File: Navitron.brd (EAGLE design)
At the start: 70 x 70 mm, 92 parts, among them J2 DX07S016JA1R1500, Q1 ROHM_RUM002N02T2LROHM_RUM002N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, Q2 2.5A/30V, Q3 ROHM_RUM002N02T2LROHM_RUM002N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, Q4 ROHM_RUM002N02T2LROHM_RUM002N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, Q5 ROHM_RUM002N02T2LROHM_RUM002N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, T1 BC847, T2 BC847, U3 MCP73831, U5 CH340C

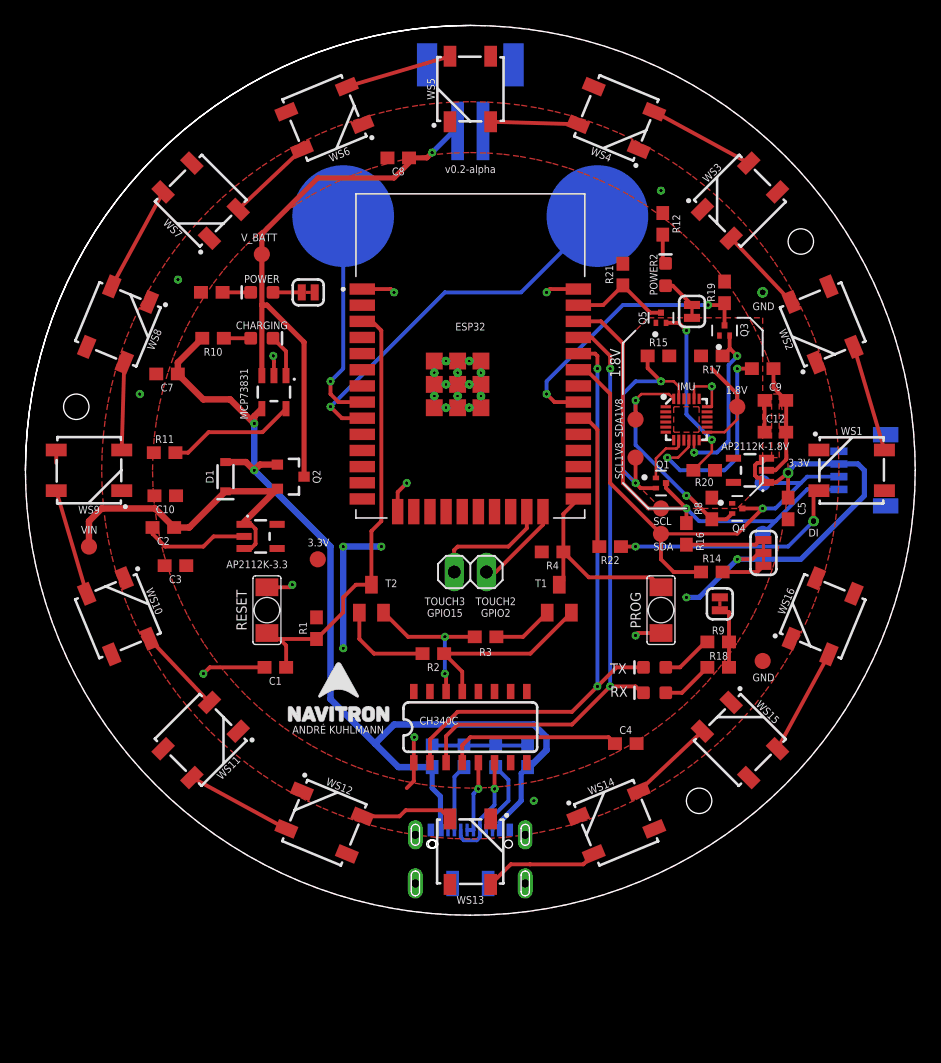
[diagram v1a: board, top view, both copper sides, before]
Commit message: Add Additional 1.8V SDA and SCL Pad
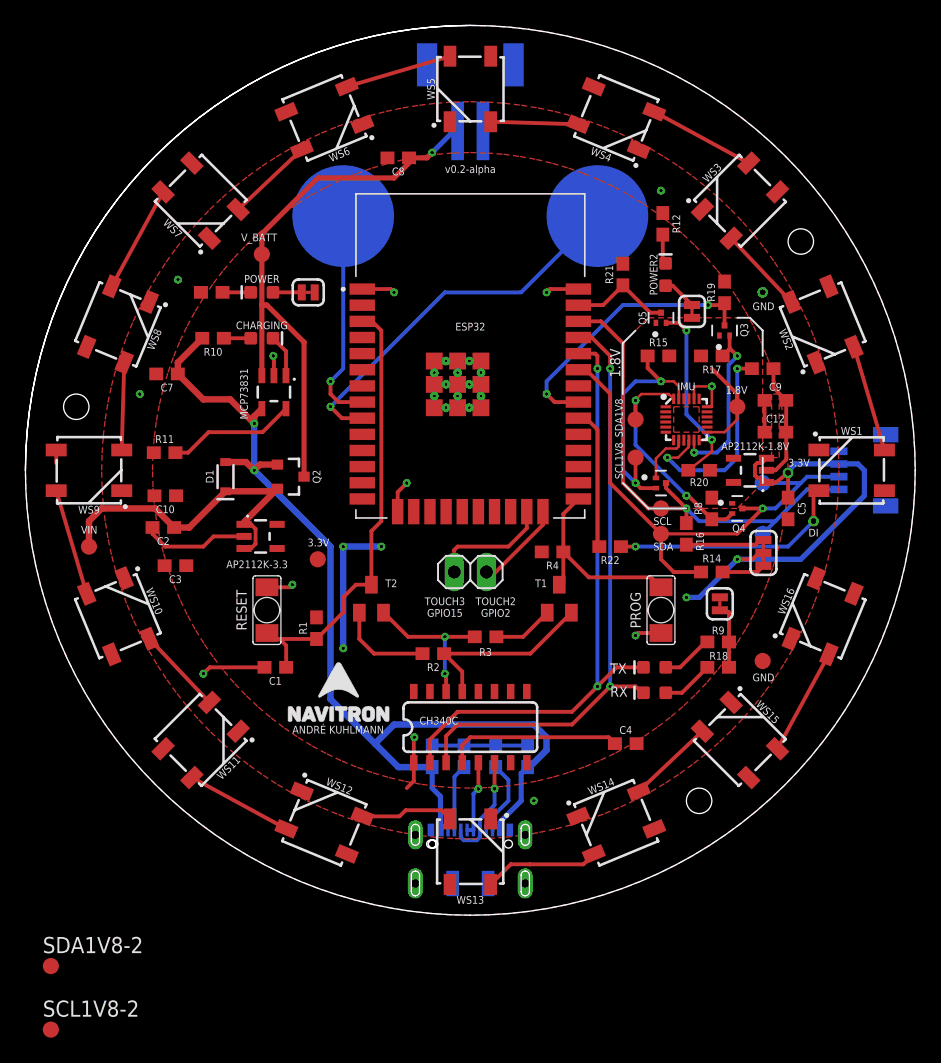
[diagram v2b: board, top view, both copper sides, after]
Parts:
- added SCL1V8-2, SDA1V8-2: PTR1B1,27, testpad:B1,27
- moved R20 0.40 mm to (53.0, 35.0)
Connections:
- net SCL1V8: now also SCL1V8-2.TP
- net SDA1V8: now also SDA1V8-2.TP
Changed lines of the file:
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@@
 <grid distance="1" unitdist="mm" unit="mm" style="lines" multiple="1" display="yes" altdistance="5" altunitdist="mil" altunit="mil"/>
 <layers>
-<layer number="1" name="Top" color="4" fill="1" visible="yes" active="yes"/>
+<layer number="1" name="Top" color="4" fill="1" visible="no" active="yes"/>
 <layer number="2" name="Route2" color="16" fill="1" visible="no" active="no"/>
 <layer number="3" name="Route3" color="17" fill="1" visible="no" active="no"/>
@@
 <layer number="19" name="Unrouted" color="6" fill="1" visible="yes" active="yes"/>
 <layer number="20" name="Dimension" color="24" fill="1" visible="yes" active="yes"/>
-<layer number="21" name="tPlace" color="7" fill="1" visible="yes" active="yes"/>
-<layer number="22" name="bPlace" color="7" fill="1" visible="no" active="yes"/>
-<layer number="23" name="tOrigins" color="15" fill="1" visible="yes" active="yes"/>
-<layer number="24" name="bOrigins" color="15" fill="1" visible="no" active="yes"/>
-<layer number="25" name="tNames" color="7" fill="1" visible="yes" active="yes"/>
-<layer number="26" name="bNames" color="7" fill="1" visible="no" active="yes"/>
+<layer number="21" name="tPlace" color="7" fill="1" visible="no" active="yes"/>
+<layer number="22" name="bPlace" color="7" fill="1" visible="yes" active="yes"/>
+<layer number="23" name="tOrigins" color="15" fill="1" visible="no" active="yes"/>
+<layer number="24" name="bOrigins" color="15" fill="1" visible="yes" active="yes"/>
+<layer number="25" name="tNames" color="7" fill="1" visible="no" active="yes"/>
+<layer number="26" name="bNames" color="7" fill="1" visible="yes" active="yes"/>
 <layer number="27" name="tValues" color="7" fill="1" visible="no" active="yes"/>
 <layer number="28" name="bValues" color="7" fill="1" visible="no" active="yes"/>
@@
 <layer number="37" name="tTest" color="7" fill="1" visible="no" active="yes"/>
 <layer number="38" name="bTest" color="7" fill="1" visible="no" active="yes"/>
-<layer number="39" name="tKeepout" color="4" fill="11" visible="yes" active="yes"/>
-<layer number="40" name="bKeepout" color="1" fill="11" visible="no" active="yes"/>
-<layer number="41" name="tRestrict" color="4" fill="10" visible="yes" active="yes"/>
-<layer number="42" name="bRestrict" color="1" fill="10" visible="no" active="yes"/>
+<layer number="39" name="tKeepout" color="4" fill="11" visible="no" active="yes"/>
+<layer number="40" name="bKeepout" color="1" fill="11" visible="yes" active="yes"/>
+<layer number="41" name="tRestrict" color="4" fill="10" visible="no" active="yes"/>
+<layer number="42" name="bRestrict" color="1" fill="10" visible="yes" active="yes"/>
 <layer number="43" name="vRestrict" color="2" fill="10" visible="no" active="yes"/>
 <layer number="44" name="Drills" color="7" fill="1" visible="no" active="yes"/>
@@
 <layer number="49" name="Reference" color="7" fill="1" visible="no" active="yes"/>
 <layer number="50" name="dxf" color="7" fill="1" visible="no" active="no"/>
-<layer number="51" name="tDocu" color="7" fill="1" visible="yes" active="yes"/>
-<layer number="52" name="bDocu" color="7" fill="1" visible="no" active="yes"/>
+<layer number="51" name="tDocu" color="7" fill="1" visible="no" active="yes"/>
+<layer number="52" name="bDocu" color="7" fill="1" visible="yes" active="yes"/>
 <layer number="53" name="tGND_GNDA" color="7" fill="9" visible="no" active="no"/>
 <layer number="54" name="bGND_GNDA" color="1" fill="9" visible="no" active="no"/>
@@
 <wire x1="47" y1="34" x2="49" y2="32" width="0.15" layer="25"/>
 <wire x1="49" y1="32" x2="52" y2="32" width="0.15" layer="25"/>
-<wire x1="57" y1="33" x2="58" y2="34" width="0.15" layer="25"/>
 <wire x1="58" y1="34" x2="58" y2="36" width="0.15" layer="25"/>
 <wire x1="56" y1="47" x2="57" y2="47" width="0.15" layer="25"/>
@@
 <attribute name="MOUSER_PART_NUMBER" value="755-RUM002N02T2L" x="50" y="34" size="1.778" layer="27" display="off"/>
 <attribute name="MPN" value="RUM002N02T2L" x="50" y="34" size="1.778" layer="27" display="off"/>
-<attribute name="NAME" x="49.6" y="35.15" size="0.6096" layer="25" ratio="20"/>
 <attribute name="PACKAGE" value="SOT-23" x="50" y="34" size="1.778" layer="27" display="off"/>
 <attribute name="PREFIX" value="Q" x="50" y="34" size="1.778" layer="27" display="off"/>
@@
 <attribute name="VALUE" x="51.238" y="30" size="0.6096" layer="27" font="vector" ratio="20" rot="R270" align="top-center"/>
 </element>
-<element name="R20" library="SparkFun-Resistors" package="0603" value="2.2k" x="53.4" y="35" smashed="yes">
-<attribute name="NAME" x="53.4" y="33.762" size="0.6096" layer="25" font="vector" ratio="20" align="bottom-center"/>
-<attribute name="PROD_ID" value="RES-12083" x="53.4" y="35" size="1.778" layer="27" display="off"/>
-<attribute name="VALUE" x="53.4" y="34.238" size="0.6096" layer="27" font="vector" ratio="20" align="top-center"/>
+<element name="R20" library="SparkFun-Resistors" package="0603" value="2.2k" x="53" y="35" smashed="yes">
+<attribute name="NAME" x="53" y="33.762" size="0.6096" layer="25" font="vector" ratio="20" align="bottom-center"/>
+<attribute name="PROD_ID" value="RES-12083" x="53" y="35" size="1.778" layer="27" display="off"/>
+<attribute name="VALUE" x="53" y="34.238" size="0.6096" layer="27" font="vector" ratio="20" align="top-center"/>
 </element>
 <element name="R21" library="SparkFun-Resistors" package="0603" value="2.2k" x="47" y="50.4" smashed="yes" rot="R90">
@@
 <attribute name="POPULARITY" value="98" x="35" y="27" size="0.6096" layer="27" ratio="20" rot="R180" display="off"/>
 <attribute name="VALUE" x="37.54" y="30.175" size="1.27" layer="27" rot="R180"/>
+</element>
+<element name="SDA1V8-2" library="testpad" library_urn="urn:adsk.eagle:library:385" package="B1,27" package3d_urn="urn:adsk.eagle:package:27944/2" value="PTR1B1,27" x="2" y="-4" smashed="yes">
+<attribute name="NAME" x="1.365" y="-2.984" size="1.27" layer="25" ratio="10"/>
+<attribute name="POPULARITY" value="2" x="2" y="-4" size="0.6096" layer="27" ratio="20" display="off"/>
+<attribute name="TP_SIGNAL_NAME" value="" x="1.365" y="-5.905" size="1" layer="37"/>
+<attribute name="VALUE" x="1.365" y="-4.762" size="0.0254" layer="27"/>
+</element>
+<element name="SCL1V8-2" library="testpad" library_urn="urn:adsk.eagle:library:385" package="B1,27" package3d_urn="urn:adsk.eagle:package:27944/2" value="PTR1B1,27" x="2" y="-9" smashed="yes">
+<attribute name="NAME" x="1.365" y="-7.984" size="1.27" layer="25" ratio="10"/>
+<attribute name="POPULARITY" value="2" x="2" y="-9" size="0.6096" layer="27" ratio="20" display="off"/>
+<attribute name="TP_SIGNAL_NAME" value="" x="1.365" y="-10.905" size="1" layer="37"/>
+<attribute name="VALUE" x="1.365" y="-9.762" size="0.0254" layer="27"/>
 </element>
 </elements>
@@
 <contactref element="JP3" pad="1"/>
 <contactref element="C9" pad="1"/>
-<polygon width="0.15" layer="1">
-<vertex x="49" y="47"/>
-<vertex x="58" y="47"/>
-<vertex x="58" y="34"/>
-<vertex x="56" y="32"/>
-<vertex x="50" y="32"/>
-<vertex x="47" y="35"/>
-<vertex x="47" y="45"/>
-</polygon>
 <contactref element="C12" pad="1"/>
 <contactref element="Q4" pad="1"/>
@@
 <contactref element="IMU" pad="13"/>
 <contactref element="IMU" pad="8"/>
+<wire x1="53.6256" y1="38" x2="55" y2="38" width="0.2032" layer="1"/>
+<wire x1="55" y1="38" x2="56" y2="39" width="0.2032" layer="1"/>
+<wire x1="56" y1="39" x2="56" y2="40" width="0.2032" layer="1"/>
+<polygon width="0.15" layer="1">
+<vertex x="47" y="45"/>
+<vertex x="49" y="47"/>
+<vertex x="57" y="47"/>
+<vertex x="58" y="46"/>
+<vertex x="58" y="34"/>
+<vertex x="56" y="32"/>
+<vertex x="49" y="32"/>
+<vertex x="47" y="34"/>
+</polygon>
 <wire x1="51.4" y1="37.3744" x2="51.379" y2="37.3534" width="0.2032" layer="1"/>
 <wire x1="51.379" y1="37.3534" x2="51.379" y2="36.8627875" width="0.2032" layer="1"/>
@@
 <wire x1="49.6" y1="35.92335625" x2="49.6" y2="34.4" width="0.2032" layer="1"/>
 <wire x1="51.2302125" y1="36.714" x2="50.39064375" y2="36.714" width="0.2032" layer="1"/>
-<wire x1="53.6256" y1="38" x2="55" y2="38" width="0.2032" layer="1"/>
-<wire x1="55" y1="38" x2="56" y2="39" width="0.2032" layer="1"/>
-<wire x1="56" y1="39" x2="56" y2="40" width="0.2032" layer="1"/>
 </signal>
 <signal name="N$8">
@@
 <wire x1="48.4475" y1="41" x2="48" y2="40.5525" width="0.2032" layer="1"/>
 <wire x1="50.625603125" y1="41" x2="48.4475" y2="41" width="0.2032" layer="1"/>
+<contactref element="SDA1V8-2" pad="TP"/>
+<wire x1="2" y1="-4" x2="52" y2="33" width="0" layer="19" extent="1-1"/>
 </signal>
 <signal name="SCL1V8">
@@
 <wire x1="51.4" y1="41.6" x2="51" y2="42" width="0.2032" layer="1"/>
 <wire x1="51" y1="42" x2="50" y2="42" width="0.2032" layer="1"/>
+<contactref element="SCL1V8-2" pad="TP"/>
+<wire x1="2" y1="-9" x2="48" y2="34" width="0" layer="19" extent="1-1"/>
 </signal>
 <signal name="DI">
@@
 <wire x1="53.938196875" y1="37.3744" x2="53" y2="37.3744" width="0.2032" layer="1"/>
 <wire x1="54" y1="37.4" x2="54" y2="36.45" width="0.2032" layer="1"/>
-<wire x1="54" y1="36.45" x2="52.55" y2="35" width="0.2032" layer="1"/>
+<wire x1="54" y1="36.45" x2="52.15" y2="35" width="0.2032" layer="1"/>
 </signal>
 <signal name="FSYNC_VIN">

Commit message: Change Bottom Logo Position
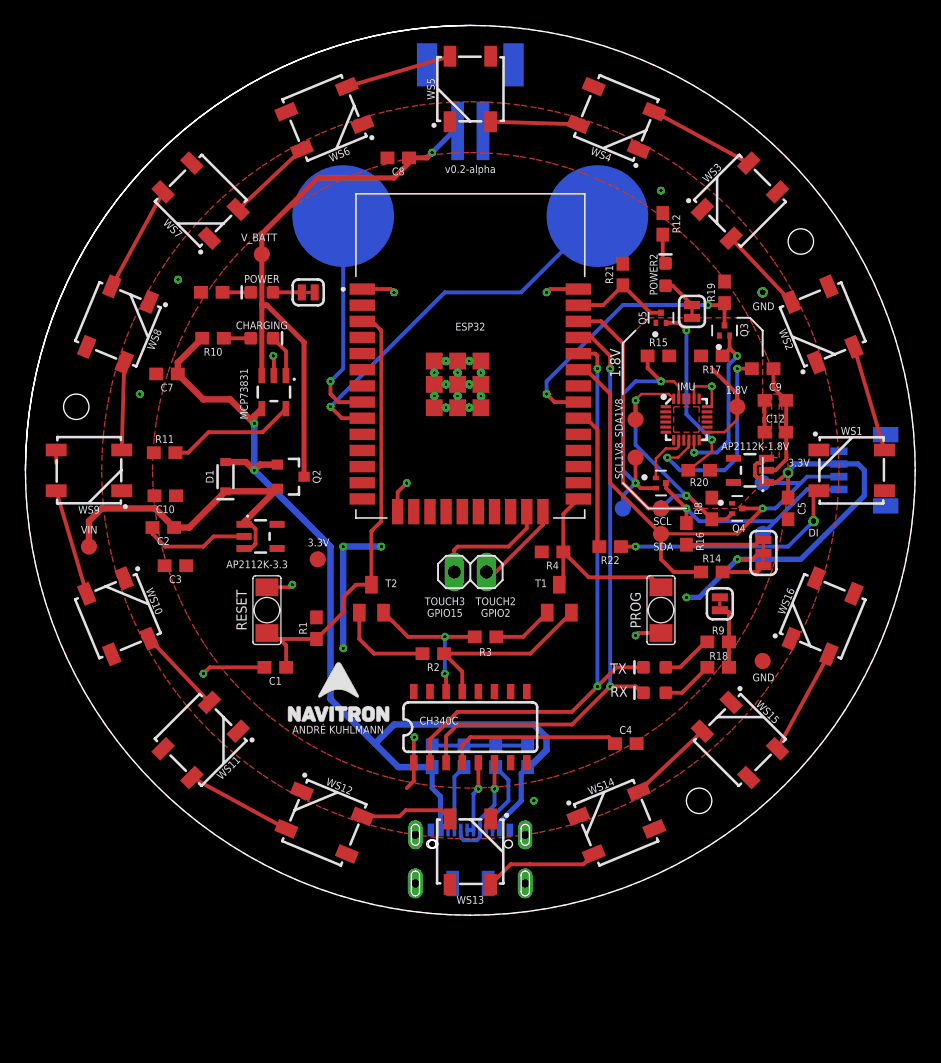
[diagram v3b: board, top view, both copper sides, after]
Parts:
- moved SCL1V8-2 60.9 mm to (47.0, 32.0), flipped to the bottom
- moved SDA1V8-2 60.0 mm to (50.0, 32.0), flipped to the bottom
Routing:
- net SDA1V8: track 18.6 -> 21.0 mm
- net SCL1V8: track 19.6 -> 22.0 mm
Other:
- board text added: "SCL1.8"
- board text added: "SDA1.8"

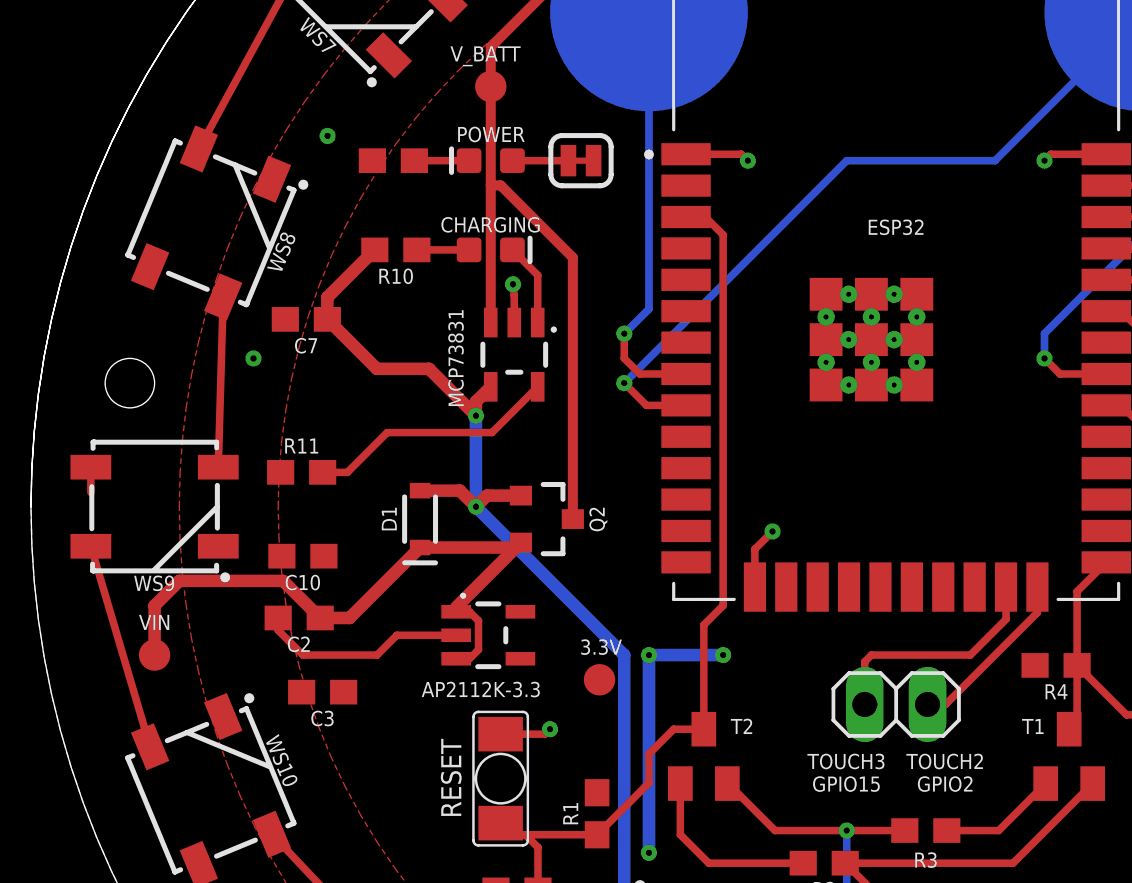
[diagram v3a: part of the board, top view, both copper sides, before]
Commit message: Cleanup 3.3V Power Circuit
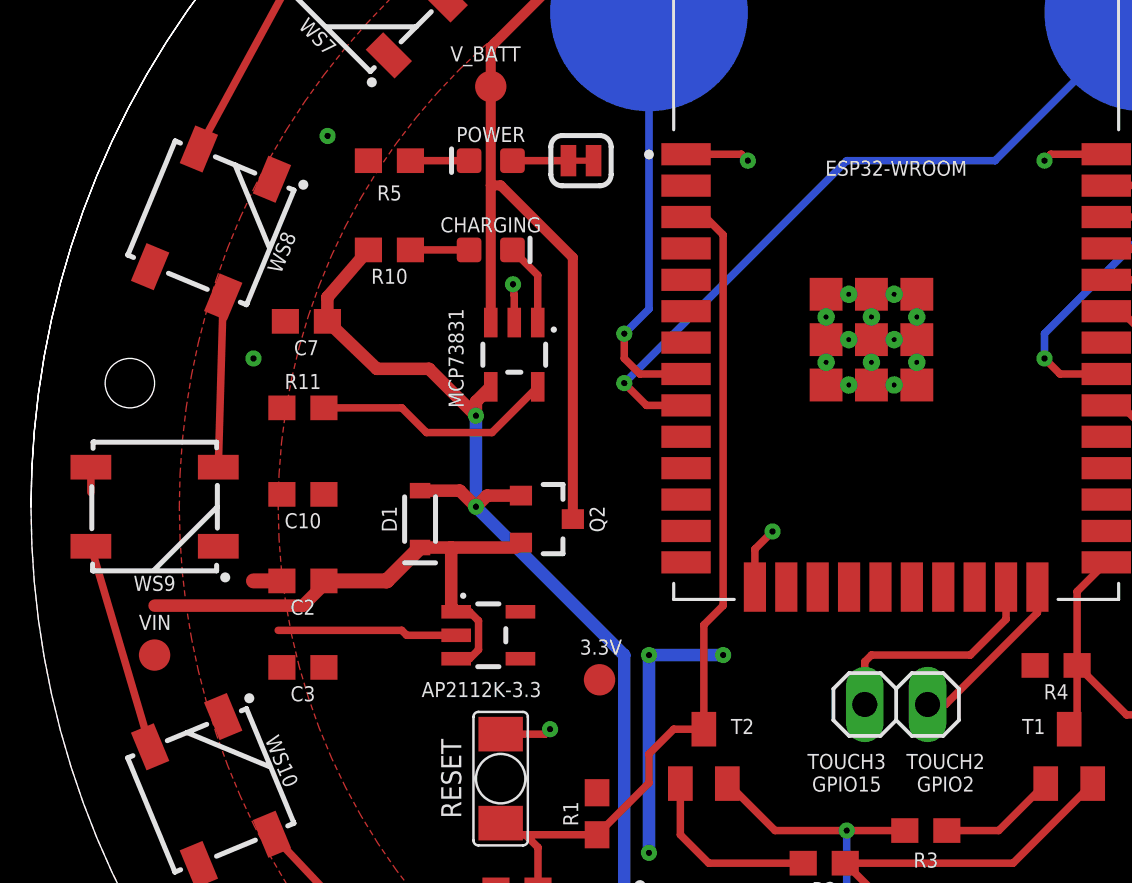
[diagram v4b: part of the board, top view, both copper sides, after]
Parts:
- moved R11 2.61 mm to (11.0, 39.0)
- moved C10 2.50 mm to (11.0, 35.5)
- moved C2 1.51 mm to (11.0, 32.0)
- moved C3 1.28 mm to (11.0, 28.5)
- moved R10 0.26 mm to (14.5, 45.4)
- moved R5 0.16 mm to (14.5, 49.0)
- moved C7 0.08 mm to (11.1, 42.5)
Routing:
- net VIN: track 27.3 -> 23.0 mm
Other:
- board text added: "ESP32-WROOM"
- board text added: "R5"

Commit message: Small changes
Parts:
- CHARGING: value RED -> GREEN
- RX1, TX1: value YELLOW -> BLUE
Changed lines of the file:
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@@
 <drawing>
 <settings>
-<setting alwaysvectorfont="yes"/>
+<setting alwaysvectorfont="no"/>
 <setting verticaltext="up"/>
 </settings>
@@
 <attribute name="VALUE" x="59" y="39.738" size="0.6096" layer="27" font="vector" ratio="20" align="top-center"/>
 </element>
-<element name="CHARGING" library="SparkFun-LED" package="LED-0603" value="RED" x="18.6" y="45.39" smashed="yes">
+<element name="CHARGING" library="SparkFun-LED" package="LED-0603" value="GREEN" x="18.6" y="45.39" smashed="yes">
 <attribute name="NAME" x="18.6" y="46.1" size="0.6096" layer="25" font="vector" ratio="20" align="bottom-center"/>
 <attribute name="PROD_ID" value="DIO-00819" x="54.16" y="-27" size="1.778" layer="27" display="off"/>
@@
 <attribute name="PROD_ID" value="RES-08283" x="-10.27" y="90.08" size="1.778" layer="27" rot="R180" display="off"/>
 </element>
-<element name="RX1" library="SparkFun-LED" package="LED-0603" value="YELLOW" x="49.5" y="19.5" smashed="yes" rot="R180">
+<element name="RX1" library="SparkFun-LED" package="LED-0603" value="BLUE" x="49.5" y="19.5" smashed="yes" rot="R180">
 <attribute name="PROD_ID" value="DIO-00819" x="5.05" y="91.89" size="1.778" layer="27" rot="R180" display="off"/>
 </element>
@@
 <attribute name="POPULARITY" value="5" x="45" y="-10.66" size="1.778" layer="27" display="off"/>
 </element>
-<element name="TX1" library="SparkFun-LED" package="LED-0603" value="YELLOW" x="49.5" y="17.5" smashed="yes" rot="R180">
+<element name="TX1" library="SparkFun-LED" package="LED-0603" value="BLUE" x="49.5" y="17.5" smashed="yes" rot="R180">
 <attribute name="PROD_ID" value="DIO-00819" x="1.24" y="89.89" size="1.778" layer="27" rot="R180" display="off"/>
 </element>
